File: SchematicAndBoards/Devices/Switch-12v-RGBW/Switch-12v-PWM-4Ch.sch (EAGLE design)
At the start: 66 parts, among them IC1 REG1117, IC2 IR4427S, IC3 IR4427S, Q1 IRF7805, Q2 IRF7805, Q3 IRF7805, Q4 IRF7805

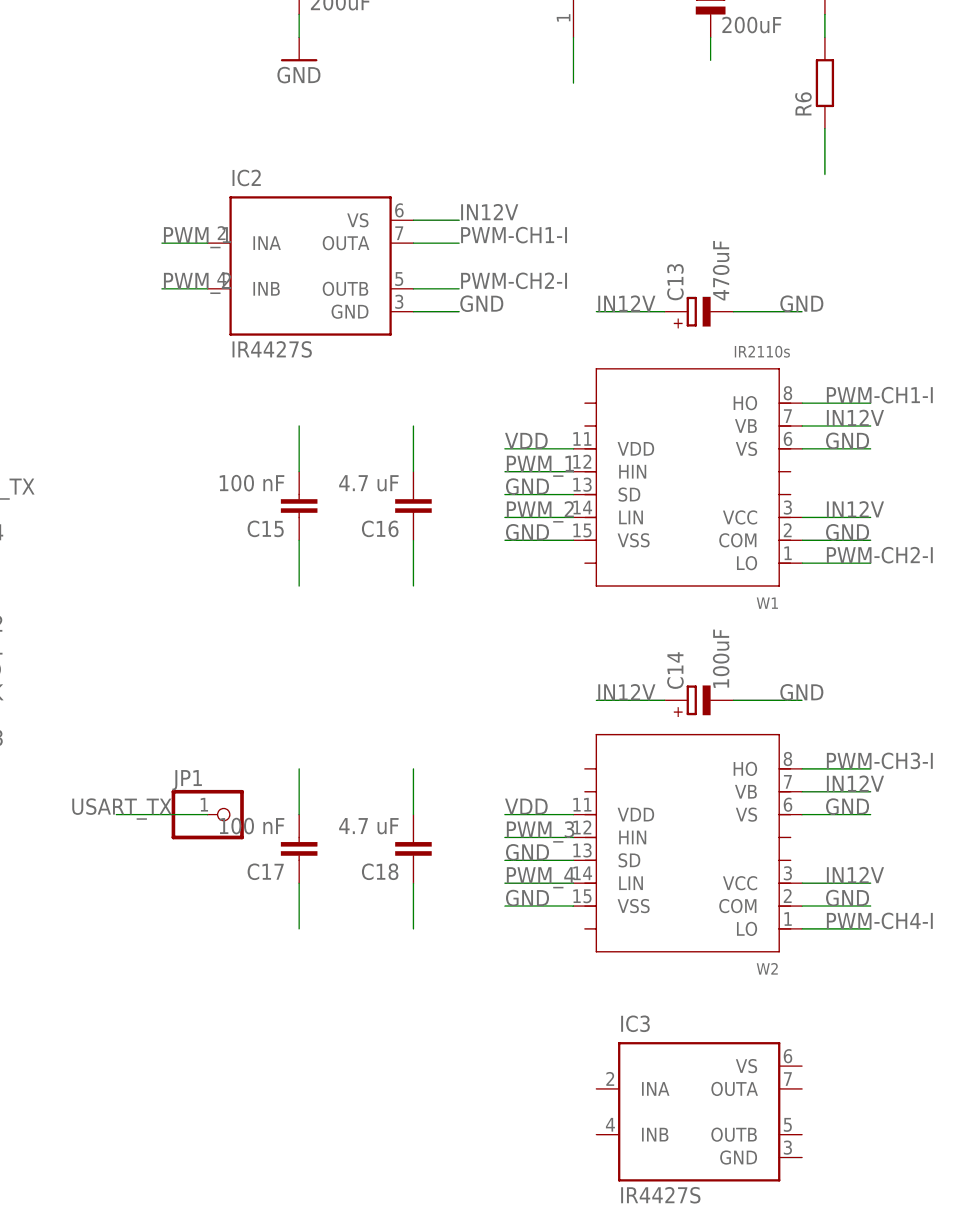
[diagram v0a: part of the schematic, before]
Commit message: Update Switch-12v-PWM-4Ch
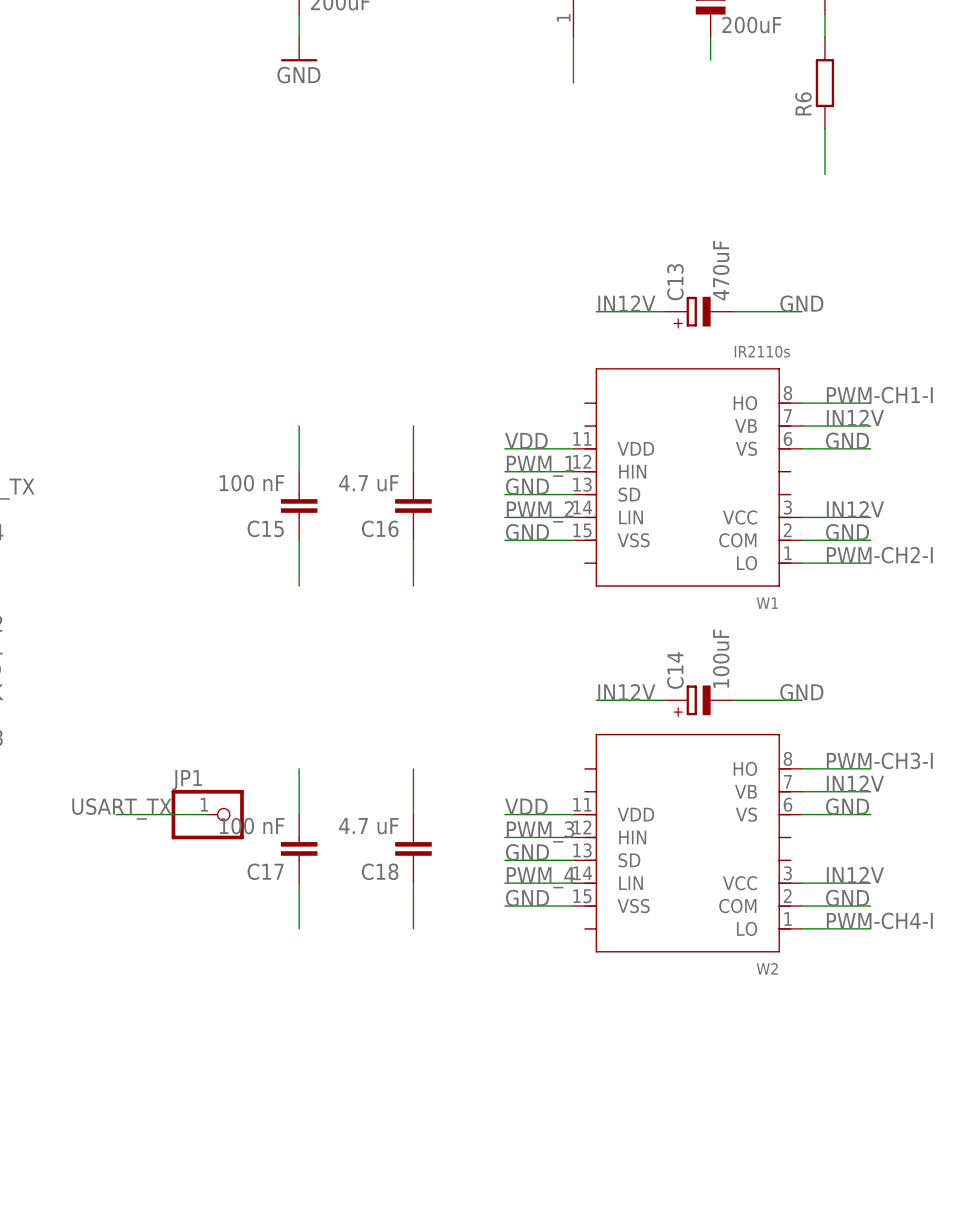
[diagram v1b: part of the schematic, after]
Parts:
- removed IC2, IC3: IR4427S, ir:IR4427S
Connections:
- net GND: no longer IC2.GND
- net IN12V: no longer IC2.VS
- net PWM-CH1-I: no longer IC2.OUTA
- net PWM-CH2-I: no longer IC2.OUTB
- net PWM_1: no longer IC2.INA
- net PWM_2: no longer IC2.INB
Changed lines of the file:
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@@
 <part name="JP2" library="pinhead" deviceset="PINHD-1X2" device=""/>
 <part name="JP3" library="pinhead" deviceset="PINHD-1X1" device=""/>
-<part name="IC2" library="ir" deviceset="IR4427" device="S"/>
-<part name="IC3" library="ir" deviceset="IR4427" device="S"/>
 </parts>
 <sheets>
@@
 <instance part="JP2" gate="G$1" x="88.9" y="76.2"/>
 <instance part="JP3" gate="G$1" x="5.08" y="53.34" rot="R180"/>
-<instance part="IC2" gate="P" x="127" y="81.28"/>
-<instance part="IC3" gate="P" x="170.18" y="-12.7"/>
 </instances>
 <busses>
@@
 <wire x1="86.36" y1="76.2" x2="76.2" y2="76.2" width="0.1524" layer="91"/>
 <label x="76.2" y="76.2" size="1.778" layer="95"/>
-</segment>
-<segment>
-<pinref part="IC2" gate="P" pin="GND"/>
-<wire x1="139.7" y1="76.2" x2="144.78" y2="76.2" width="0.1524" layer="91"/>
-<label x="144.78" y="76.2" size="1.778" layer="95"/>
 </segment>
 </net>
@@
 <label x="325.12" y="53.34" size="1.778" layer="95"/>
 </segment>
-<segment>
-<pinref part="IC2" gate="P" pin="VS"/>
-<wire x1="139.7" y1="86.36" x2="144.78" y2="86.36" width="0.1524" layer="91"/>
-<label x="144.78" y="86.36" size="1.778" layer="95"/>
-</segment>
 </net>
 <net name="PWM_1" class="0">
@@
 <wire x1="78.74" y1="38.1" x2="86.36" y2="38.1" width="0.1524" layer="91"/>
 <label x="86.36" y="38.1" size="1.778" layer="95"/>
-</segment>
-<segment>
-<pinref part="IC2" gate="P" pin="INA"/>
-<wire x1="116.84" y1="83.82" x2="111.76" y2="83.82" width="0.1524" layer="91"/>
-<label x="111.76" y="83.82" size="1.778" layer="95"/>
 </segment>
 </net>
@@
 <label x="86.36" y="40.64" size="1.778" layer="95"/>
 </segment>
-<segment>
-<pinref part="IC2" gate="P" pin="INB"/>
-<wire x1="116.84" y1="78.74" x2="111.76" y2="78.74" width="0.1524" layer="91"/>
-<label x="111.76" y="78.74" size="1.778" layer="95"/>
-</segment>
 </net>
 <net name="VDD5" class="0">
@@
 <label x="185.42" y="66.04" size="1.778" layer="95"/>
 </segment>
-<segment>
-<pinref part="IC2" gate="P" pin="OUTA"/>
-<wire x1="139.7" y1="83.82" x2="144.78" y2="83.82" width="0.1524" layer="91"/>
-<label x="144.78" y="83.82" size="1.778" layer="95"/>
-</segment>
 </net>
 <net name="PWM-CH3-I" class="0">
@@
 <label x="185.42" y="48.26" size="1.778" layer="95"/>
 </segment>
-<segment>
-<pinref part="IC2" gate="P" pin="OUTB"/>
-<wire x1="139.7" y1="78.74" x2="144.78" y2="78.74" width="0.1524" layer="91"/>
-<label x="144.78" y="78.74" size="1.778" layer="95"/>
-</segment>
-</net>
+</net>

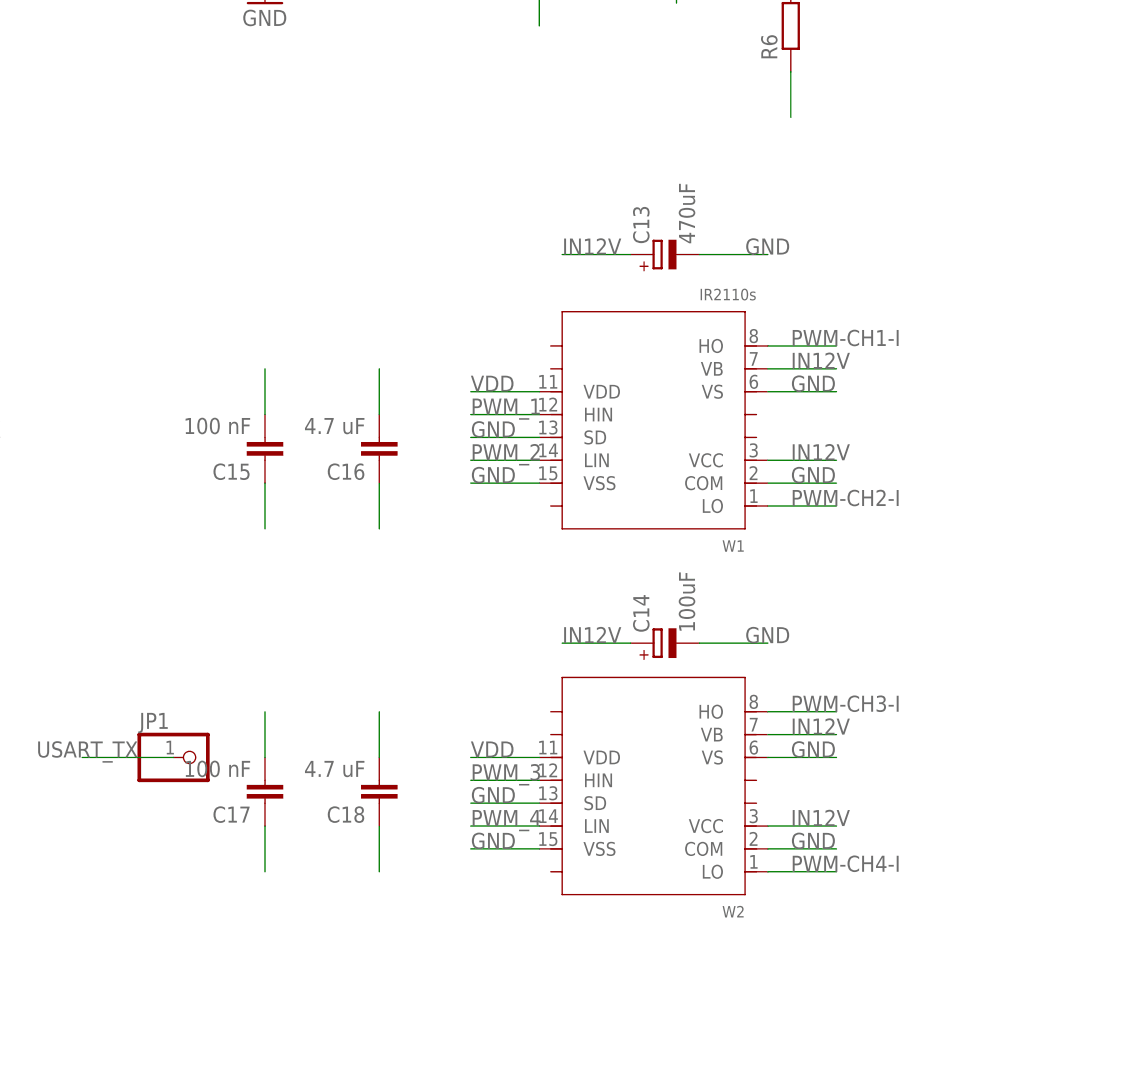
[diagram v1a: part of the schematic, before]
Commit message: Update Switch-12v-PWM-4Ch - replace driver to IR4427S
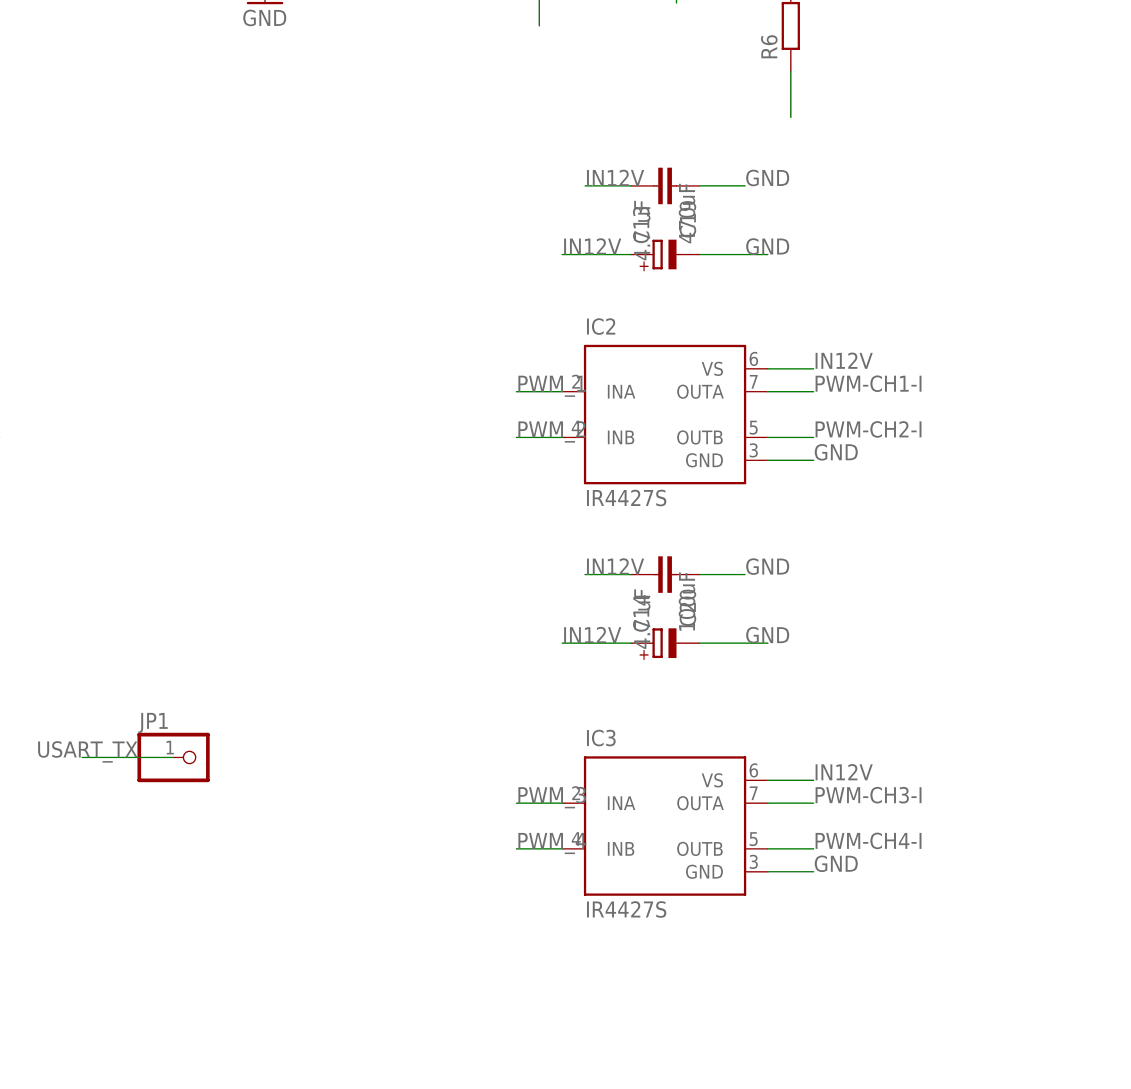
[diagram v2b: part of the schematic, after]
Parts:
- removed C15, C17: 100 nF, resistor:C-EUC0805
- removed C16, C18: 4.7 uF, resistor:C-EUC0805
- removed W1: IR2110s, my_components:IR2110
- removed W2: (no value), my_components:IR2110
- added C19, C20: 4.7 uF, resistor:C-EUC0805
- added IC2, IC3: IR4427S, ir:IR4427S
- C13, C14: device resistor:CPOL-EU153CLV-0605 -> resistor:CPOL-EU085CS-1AR
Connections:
- net GND: now also C19.1, C20.1, IC2.GND, IC3.GND; no longer C15.1, C16.1, C17.1, C18.1, W1.COM, W1.SD, W1.VS, W1.VSS, W2.COM, W2.SD, W2.VS, W2.VSS
- net IN12V: now also C19.2, C20.2, IC2.VS, IC3.VS; no longer W1.VB, W1.VCC, W2.VB, W2.VCC
- net PWM-CH1-I: now also IC2.OUTA; no longer W1.HO
- net PWM-CH2-I: now also IC2.OUTB; no longer W1.LO
- net PWM-CH3-I: now also IC3.OUTA; no longer W2.HO
- net PWM-CH4-I: now also IC3.OUTB; no longer W2.LO
- net PWM_1: now also IC2.INA; no longer W1.HIN
- net PWM_2: now also IC2.INB; no longer W1.LIN
- net PWM_3: now also IC3.INA; no longer W2.HIN
- net PWM_4: now also IC3.INB; no longer W2.LIN
- net VDD: no longer C15.2, C16.2, C17.2, C18.2, W1.VDD, W2.VDD

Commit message: Update schematic and boards
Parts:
- C11, C12, C7, C8: device resistor:CPOL-EU153CLV-0807 -> resistor:CPOL-EUE5-8.5
- C2, C3, C5: device resistor:CPOL-EU153CLV-0605 -> resistor:CPOL-EUSMCC
- D4, D5, D7, D9: device diode:DIODE-DO-214AC -> diode:DIODE-D-7.5
- L2, L3, L4, L5: value DR74 -> 82114R; device inductors:DR74 -> inductors:82114R
- renumbered RSC to R20, RSC1 to R21, RSC2 to R22, U$1 to U1, U$2 to U2

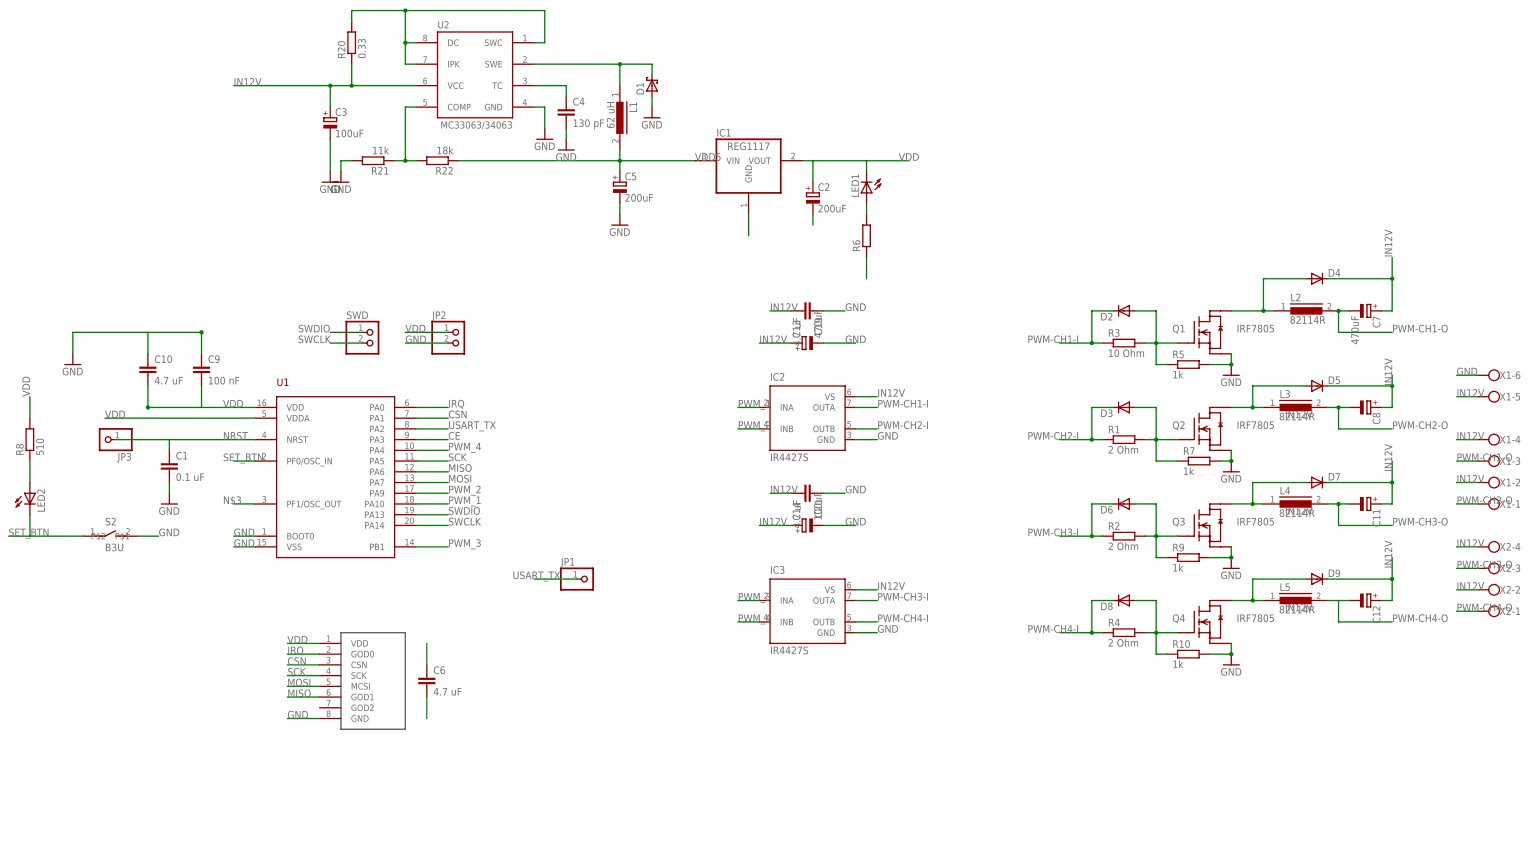
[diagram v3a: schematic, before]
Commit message: Update Switch-12v-PWM-4Ch schematic
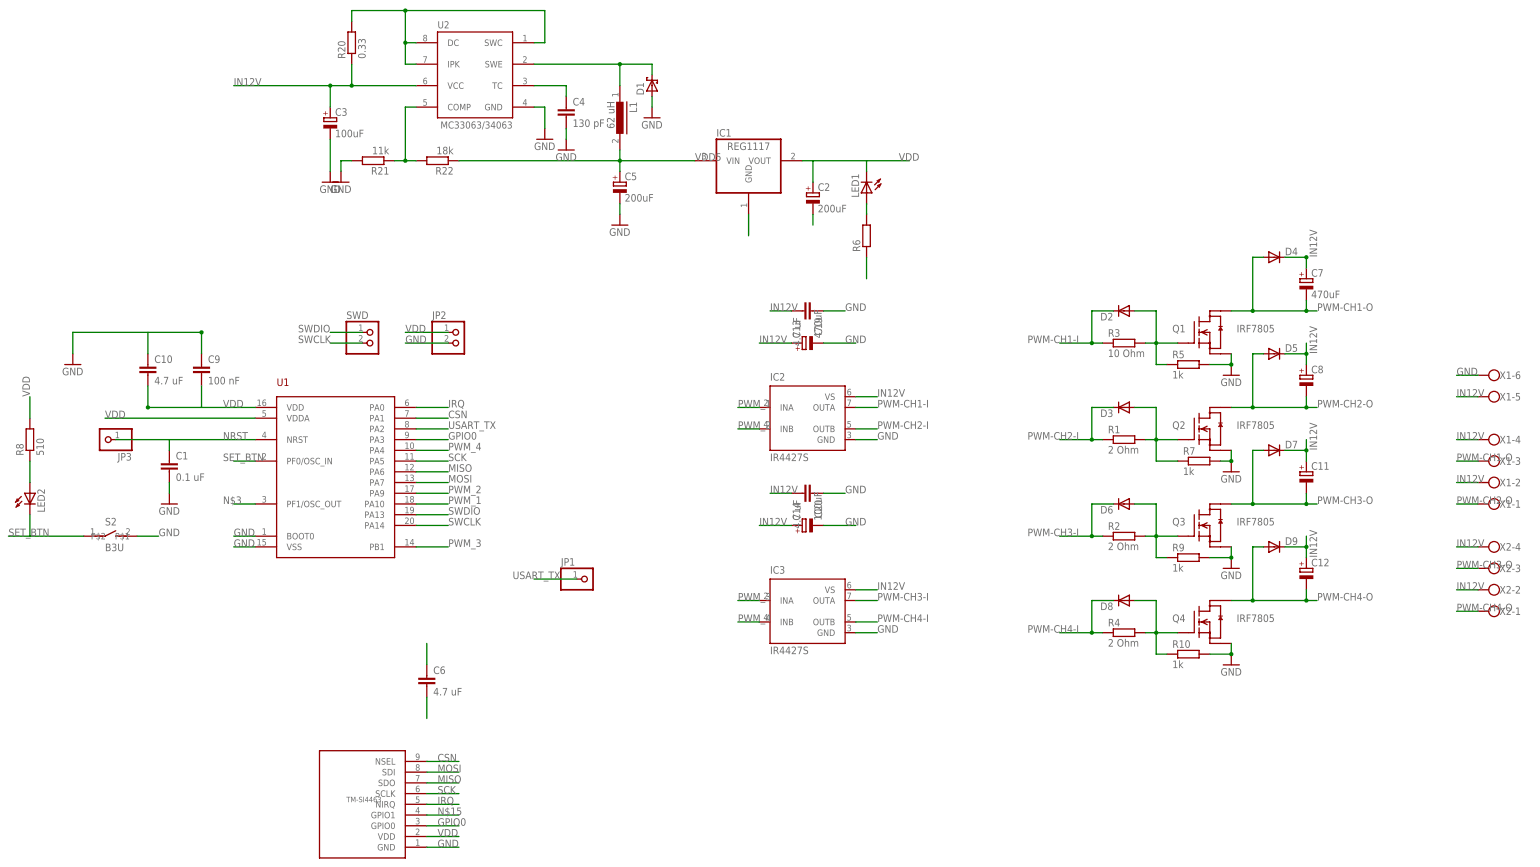
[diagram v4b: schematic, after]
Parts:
- removed L2, L3, L4, L5: 82114R, inductors:82114R
- removed U$3: AS07-M1101S, RemoteSwitchComponents:AS07-M1101S
- added U$1: TM-SI4463, RemoteSwitchComponents:TM-SI4463
- D2, D3, D6, D8: device diode:DIODE-DO-214AC -> diode:DIODE-DO214BA
- D4, D5, D7, D9: device diode:DIODE-D-7.5 -> diode:DIODE-DO214BA
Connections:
- removed net CE: U1.PA3
- removed net N$1: D4.A, L2.1, Q1.D@4
- removed net N$10: D7.A, L4.1, Q3.D@4
- removed net N$2: D5.A, L3.1, Q2.D@4
- removed net N$8: D9.A, L5.1, Q4.D@4
- new net GPIO0: U$1.GPIO0, U1.PA3
- new net N$15: U$1.GPIO1
- net CSN: now also U$1.NSEL; no longer U$3.CSN
- net GND: now also U$1.GND; no longer U$3.GND
- net IRQ: now also U$1.NIRQ; no longer U$3.GOD0
- net MISO: now also U$1.SDO; no longer U$3.GOD1
- net MOSI: now also U$1.SDI; no longer U$3.MCSI
- net PWM-CH1-O: now also D4.A, Q1.D@4; no longer L2.2
- net PWM-CH2-O: now also D5.A, Q2.D@4; no longer L3.2
- net PWM-CH3-O: now also D7.A, Q3.D@4; no longer L4.2
- net PWM-CH4-O: now also D9.A, Q4.D@4; no longer L5.2
- net SCK: now also U$1.SCLK; no longer U$3.SCK
- net VDD: now also U$1.VDD; no longer U$3.VDD
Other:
- moved on the sheet: C11, C12, C7, C8, D4, D5, D7, D9
